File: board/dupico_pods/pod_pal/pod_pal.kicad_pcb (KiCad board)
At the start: 2 copper layers, 17.4 x 53.9 mm, 8 parts, among them J1 dupico, J2 GAL, Q1 2N3906, U1 74HCT04

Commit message: Add rev.1 for the pal pod
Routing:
- net VCC: track 58.2 -> 71.6 mm, vias 0 -> 1
- net GND: track 63.2 -> 67.5 mm, vias 3 -> 4
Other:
- board text added: "PAL Pod Rev. 1"
- board text removed: "PAL Pod Rev. 0"
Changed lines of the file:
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@@
 		)
 		(fp_text user "${REFERENCE}"
-			(at 0 0 360)
+			(at 0 0 0)
 			(layer "F.Fab")
 			(effects
@@
 		)
 		(property "Value" "Force VCC"
-			(at 0 5.31 360)
+			(at 0 5.31 0)
 			(layer "F.Fab")
 			(effects
@@
 		(layer "Edge.Cuts")
 	)
-	(gr_text "PAL Pod\nRev. 0"
+	(gr_text "PAL Pod\nRev. 1"
 		(at 124.46 92.202 90)
 		(layer "B.SilkS")
@@
 	)
 	(segment
+		(start 118.11 94.9575)
+		(end 118.11 91.694)
+		(width 0.35)
+		(layer "F.Cu")
+		(net 1)
+	)
+	(segment
 		(start 128.27 90.424)
 		(end 127.254 91.44)
@@
 		(width 0.35)
 		(layer "F.Cu")
+		(net 1)
+	)
+	(via
+		(at 118.11 91.694)
+		(size 0.6)
+		(drill 0.3)
+		(layers "F.Cu" "B.Cu")
 		(net 1)
 	)
@@
 	)
 	(segment
-		(start 118.618 94.4495)
+		(start 120.65 76.2)
+		(end 120.65 94.234)
+		(width 0.35)
+		(layer "B.Cu")
+		(net 1)
+	)
+	(segment
+		(start 120.65 94.234)
+		(end 119.9265 94.9575)
+		(width 0.35)
+		(layer "B.Cu")
+		(net 1)
+	)
+	(segment
+		(start 119.9265 94.9575)
 		(end 118.11 94.9575)
 		(width 0.35)
@@
 	)
 	(segment
-		(start 120.65 89.154)
-		(end 118.618 91.186)
-		(width 0.35)
-		(layer "B.Cu")
-		(net 1)
-	)
-	(segment
-		(start 118.618 91.186)
-		(end 118.618 94.4495)
-		(width 0.35)
-		(layer "B.Cu")
-		(net 1)
-	)
-	(segment
-		(start 120.65 76.2)
-		(end 120.65 89.154)
-		(width 0.35)
-		(layer "B.Cu")
-		(net 1)
+		(start 118.11 98.044)
+		(end 118.11 98.298)
+		(width 0.35)
+		(layer "F.Cu")
+		(net 2)
 	)
 	(segment
@@
 	(segment
 		(start 118.11 98.0825)
-		(end 118.11 98.298)
+		(end 118.11 98.044)
 		(width 0.35)
 		(layer "F.Cu")
@@
 		(net 2)
 	)
+	(via
+		(at 118.11 98.044)
+		(size 0.6)
+		(drill 0.3)
+		(layers "F.Cu" "B.Cu")
+		(net 2)
+	)
+	(segment
+		(start 118.11 98.044)
+		(end 117.385 97.319)
+		(width 0.35)
+		(layer "B.Cu")
+		(net 2)
+	)
+	(segment
+		(start 119.385 91.689)
+		(end 119.385 87.635)
+		(width 0.35)
+		(layer "B.Cu")
+		(net 2)
+	)
+	(segment
+		(start 117.385 97.319)
+		(end 117.385 93.689)
+		(width 0.35)
+		(layer "B.Cu")
+		(net 2)
+	)
+	(segment
+		(start 117.385 93.689)
+		(end 119.385 91.689)
+		(width 0.35)
+		(layer "B.Cu")
+		(net 2)
+	)
+	(segment
+		(start 119.385 87.635)
+		(end 118.11 86.36)
+		(width 0.35)
+		(layer "B.Cu")
+		(net 2)
+	)

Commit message: Update pal pod for dupico
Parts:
- R1: value 2.2k -> 1k
- U1: value 74HCT04 -> 74AC04
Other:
- board text added: "PAL Pod Rev. 2"
- board text removed: "PAL Pod Rev. 1"
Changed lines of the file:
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@@
 			)
 		)
-		(property "Value" "2.2k"
+		(property "Value" "1k"
 			(at 3.048 0 180)
 			(layer "F.SilkS")
@@
 			)
 		)
-		(property "Value" "74HCT04"
+		(property "Value" "74AC04"
 			(at 0 0 90)
 			(layer "F.SilkS")
@@
 		(layer "Edge.Cuts")
 	)
-	(gr_text "PAL Pod\nRev. 1"
+	(gr_text "PAL Pod\nRev. 2"
 		(at 124.46 92.202 90)
 		(layer "B.SilkS")

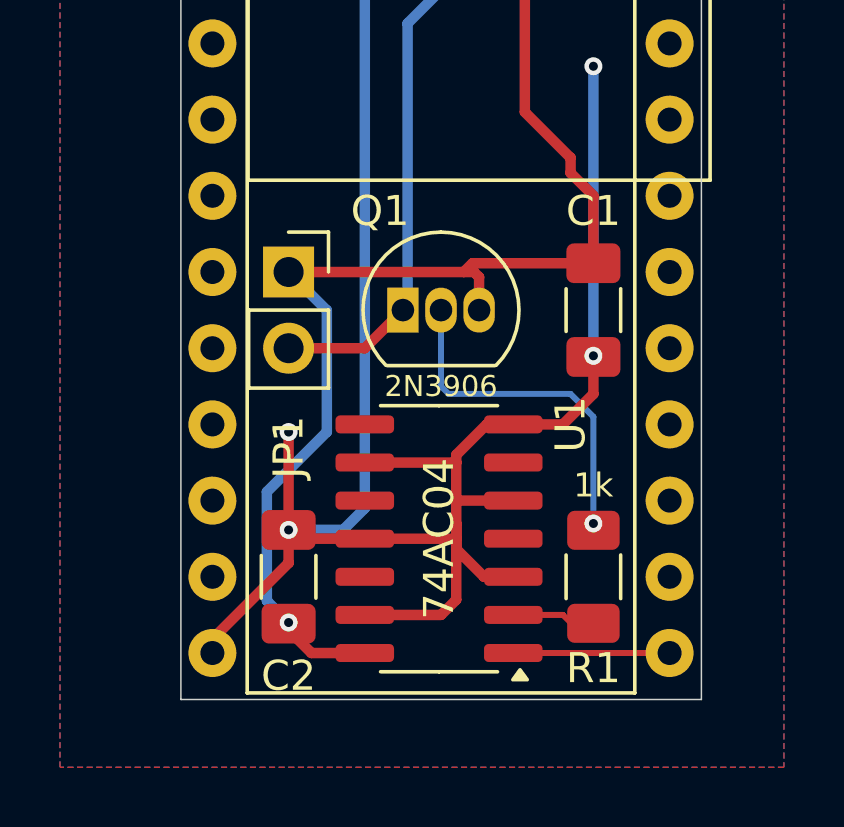
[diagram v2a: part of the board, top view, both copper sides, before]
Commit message: Fix rotated transistor in dupico pal pod
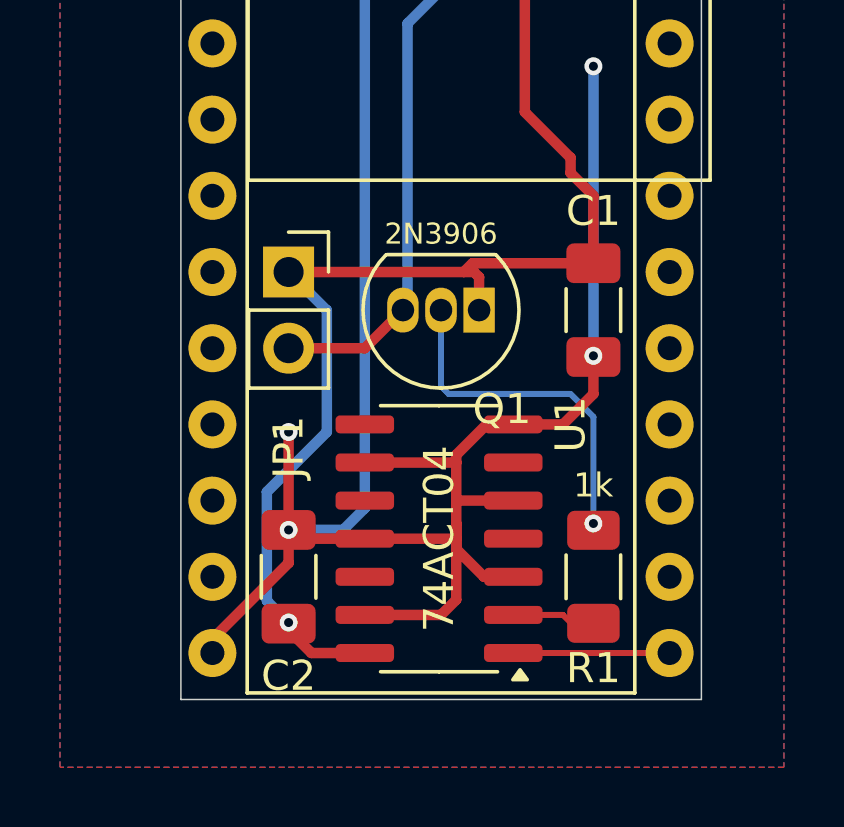
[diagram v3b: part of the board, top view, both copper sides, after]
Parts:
- U1: value 74AC04 -> 74ACT04
- moved Q1 2.54 mm to (124.5, 87.6), turned to 180 degrees
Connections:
- Q1 pad 1: /ZIF_40 -> VCC
- Q1 pad 3: VCC -> /ZIF_40
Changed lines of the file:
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@@
 	(footprint "Package_TO_SOT_THT:TO-92_Inline"
 		(layer "F.Cu")
-		(at 121.92 87.63)
+		(at 124.46 87.63 180)
 		(descr "TO-92 leads in-line, narrow, oval pads, drill 0.75mm (see NXP sot054_po.pdf)")
 		(tags "to-92 sc-43 sc-43a sot54 PA33 transistor")
 		(property "Reference" "Q1"
-			(at -0.762 -3.302 0)
+			(at -0.762 -3.302 360)
 			(layer "F.SilkS")
 			(effects
@@
 		)
 		(property "Value" "2N3906"
-			(at 1.27 2.54 0)
+			(at 1.27 2.54 360)
 			(layer "F.SilkS")
 			(effects
@@
 		)
 		(property "Footprint" "Package_TO_SOT_THT:TO-92_Inline"
-			(at 0 0 0)
+			(at 0 0 180)
 			(unlocked yes)
 			(layer "F.Fab")
@@
 		)
 		(property "Datasheet" "https://www.onsemi.com/pub/Collateral/2N3906-D.PDF"
-			(at 0 0 0)
+			(at 0 0 180)
 			(unlocked yes)
 			(layer "F.Fab")
@@
 		)
 		(property "Description" "-0.2A Ic, -40V Vce, Small Signal PNP Transistor, TO-92"
-			(at 0 0 0)
+			(at 0 0 180)
 			(unlocked yes)
 			(layer "F.Fab")
@@
 		)
 		(fp_arc
+			(start 1.27 -2.6)
+			(mid 3.672087 -0.994977)
+			(end 3.108478 1.838478)
+			(stroke
+				(width 0.12)
+				(type solid)
+			)
+			(layer "F.SilkS")
+		)
+		(fp_arc
 			(start -0.568478 1.838478)
 			(mid -1.132087 -0.994977)
@@
 			(layer "F.SilkS")
 		)
-		(fp_arc
-			(start 1.27 -2.6)
-			(mid 3.672087 -0.994977)
-			(end 3.108478 1.838478)
-			(stroke
-				(width 0.12)
-				(type solid)
-			)
-			(layer "F.SilkS")
+		(fp_line
+			(start 4 2.01)
+			(end 4 -2.73)
+			(stroke
+				(width 0.05)
+				(type solid)
+			)
+			(layer "F.CrtYd")
+		)
+		(fp_line
+			(start 4 2.01)
+			(end -1.46 2.01)
+			(stroke
+				(width 0.05)
+				(type solid)
+			)
+			(layer "F.CrtYd")
+		)
+		(fp_line
+			(start -1.46 -2.73)
+			(end 4 -2.73)
+			(stroke
+				(width 0.05)
+				(type solid)
+			)
+			(layer "F.CrtYd")
 		)
 		(fp_line
@@
 		)
 		(fp_line
-			(start -1.46 -2.73)
-			(end 4 -2.73)
-			(stroke
-				(width 0.05)
-				(type solid)
-			)
-			(layer "F.CrtYd")
-		)
-		(fp_line
-			(start 4 2.01)
-			(end -1.46 2.01)
-			(stroke
-				(width 0.05)
-				(type solid)
-			)
-			(layer "F.CrtYd")
-		)
-		(fp_line
-			(start 4 2.01)
-			(end 4 -2.73)
-			(stroke
-				(width 0.05)
-				(type solid)
-			)
-			(layer "F.CrtYd")
-		)
-		(fp_line
 			(start -0.5 1.75)
 			(end 3 1.75)
+			(stroke
+				(width 0.1)
+				(type solid)
+			)
+			(layer "F.Fab")
+		)
+		(fp_arc
+			(start 1.27 -2.48)
+			(mid 3.561221 -0.949055)
+			(end 3.023625 1.753625)
 			(stroke
 				(width 0.1)
@@
 			(layer "F.Fab")
 		)
-		(fp_arc
-			(start 1.27 -2.48)
-			(mid 3.561221 -0.949055)
-			(end 3.023625 1.753625)
-			(stroke
-				(width 0.1)
-				(type solid)
-			)
-			(layer "F.Fab")
-		)
 		(fp_text user "${REFERENCE}"
-			(at 1.27 0 0)
+			(at 1.27 0 360)
 			(layer "F.Fab")
 			(effects
@@
 		)
 		(pad "1" thru_hole rect
-			(at 0 0)
+			(at 0 0 180)
 			(size 1.05 1.5)
 			(drill 0.75)
 			(layers "*.Cu" "*.Mask")
 			(remove_unused_layers no)
-			(net 30 "/ZIF_40")
+			(net 2 "VCC")
 			(pinfunction "E")
 			(pintype "passive")
 		)
 		(pad "2" thru_hole oval
-			(at 1.27 0)
+			(at 1.27 0 180)
 			(size 1.05 1.5)
 			(drill 0.75)
@@
 		)
 		(pad "3" thru_hole oval
-			(at 2.54 0)
+			(at 2.54 0 180)
 			(size 1.05 1.5)
 			(drill 0.75)
 			(layers "*.Cu" "*.Mask")
 			(remove_unused_layers no)
-			(net 2 "VCC")
+			(net 30 "/ZIF_40")
 			(pinfunction "C")
 			(pintype "passive")
@@
 			)
 		)
-		(property "Value" "74AC04"
+		(property "Value" "74ACT04"
 			(at 0 0 90)
 			(layer "F.SilkS")
